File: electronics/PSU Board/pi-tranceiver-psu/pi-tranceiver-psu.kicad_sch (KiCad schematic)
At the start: 28 parts, among them IC1 LTC4368IMS-2#PBF, Q1 DMT6002LPS-13, Q2 DMT6002LPS-13

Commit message: Added 5.1V 3V supply
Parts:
- added C?: 10nF, Capacitor_SMD:C_0805_2012Metric_Pad1.18x1.45mm_HandSolder, symbol Device:C
- added C?: 220uF, CAPAE660X770N, symbol SamacSys_Parts:865080545012
- added D?: 1N5822, symbol Device:D_Schottky
- added L?: 33uH, symbol Device:L
- added R?: 3K16, Resistor_SMD:R_0805_2012Metric_Pad1.20x1.40mm_HandSolder, symbol Device:R
- added R?: 1K, Resistor_SMD:R_0805_2012Metric_Pad1.20x1.40mm_HandSolder, symbol Device:R
- added U?: LM2596S-ADJ, Package_TO_SOT_SMD:TO-263-5_TabPin3, symbol Regulator_Switching:LM2596S-ADJ
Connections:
- net GND: now also C?.2, D?.2 (A), R?.2, U?.3 (GND)
- net at C3.1, C5.1, D?.2 (A)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: now also U?.1 (VIN), U?.5 (~{ON}/OFF)
- new net: D?.1 (K), L?.2, U?.2 (OUT)
- new net: C?.1, R?.1, R?.1, U?.4 (FB)
- new net: C?.1, C?.2, L?.1, R?.2
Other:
- note added: "13.8V Output"
- note added: "5.117V @3A"
- note added: "Input"
- moved on the sheet: C1, C2, C3, C4, C5, C?, D1, D?, IC1, Q1, Q2, Q?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

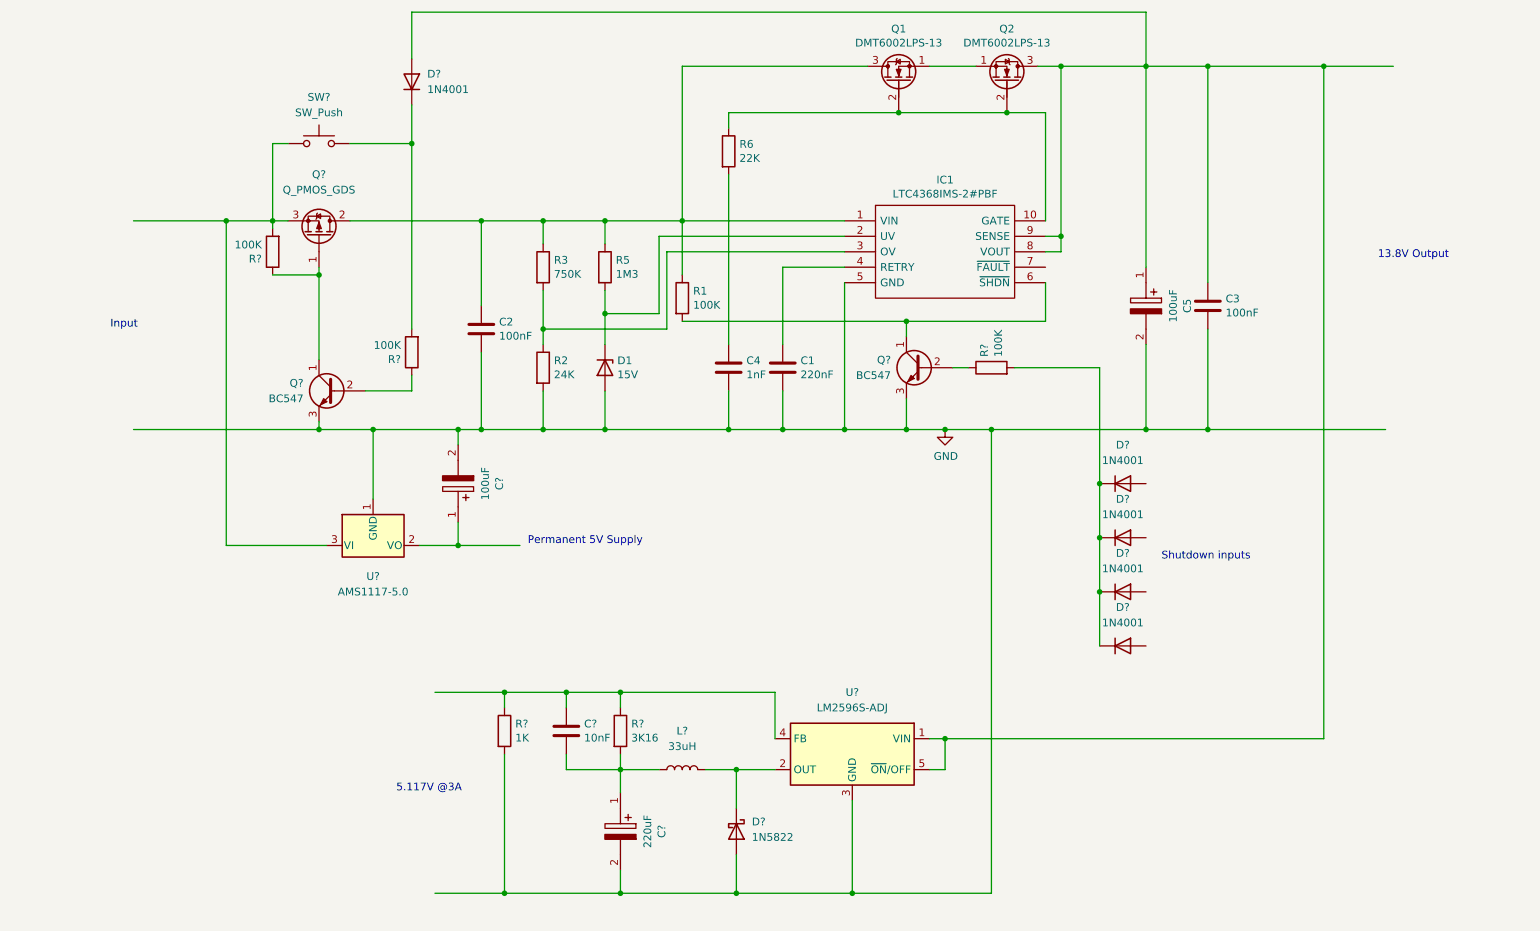
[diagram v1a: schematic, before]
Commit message: Updated shutdown circuit
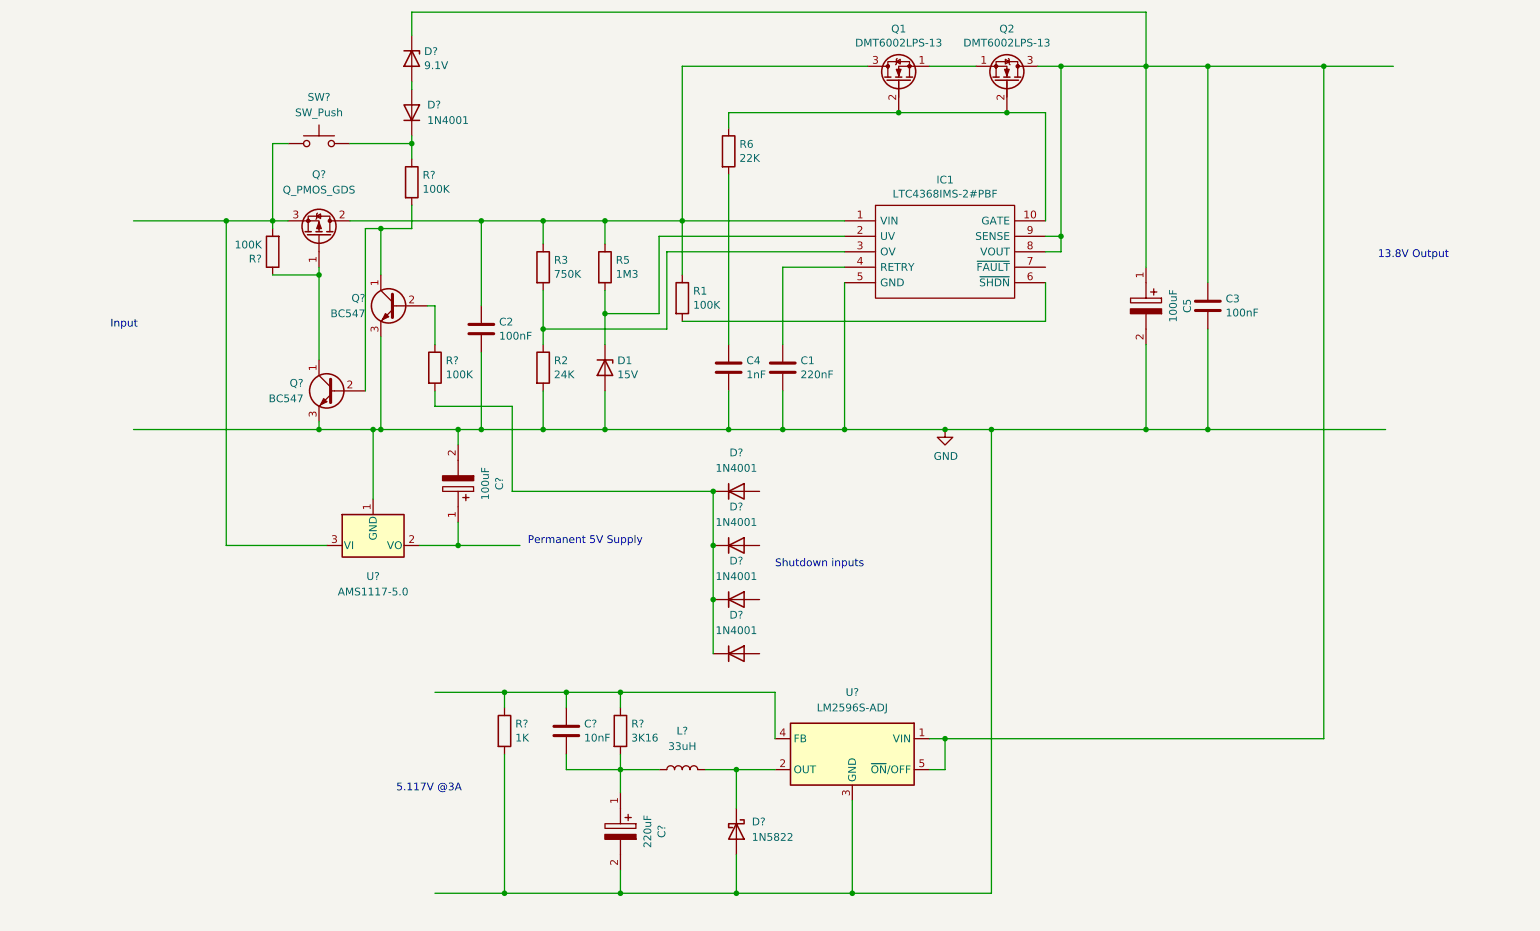
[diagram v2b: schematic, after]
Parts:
- added D?: 9.1V, Diode_SMD:D_0805_2012Metric, symbol Device:D_Zener
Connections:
- net at IC1.6 (~{SHDN}), R1.2: no longer Q?.1 (C)
- net at C3.1, C5.1, IC1.8 (VOUT)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: now also D?.1 (K); no longer D?.2 (A)
- net at R?.1: now also D?.1 (K), SW?.2; no longer Q?.2 (B)
- new net: Q?.1 (C), Q?.2 (B), R?.2
- new net: D?.2 (A), D?.2 (A)
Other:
- moved on the sheet: D?, Q?, R?

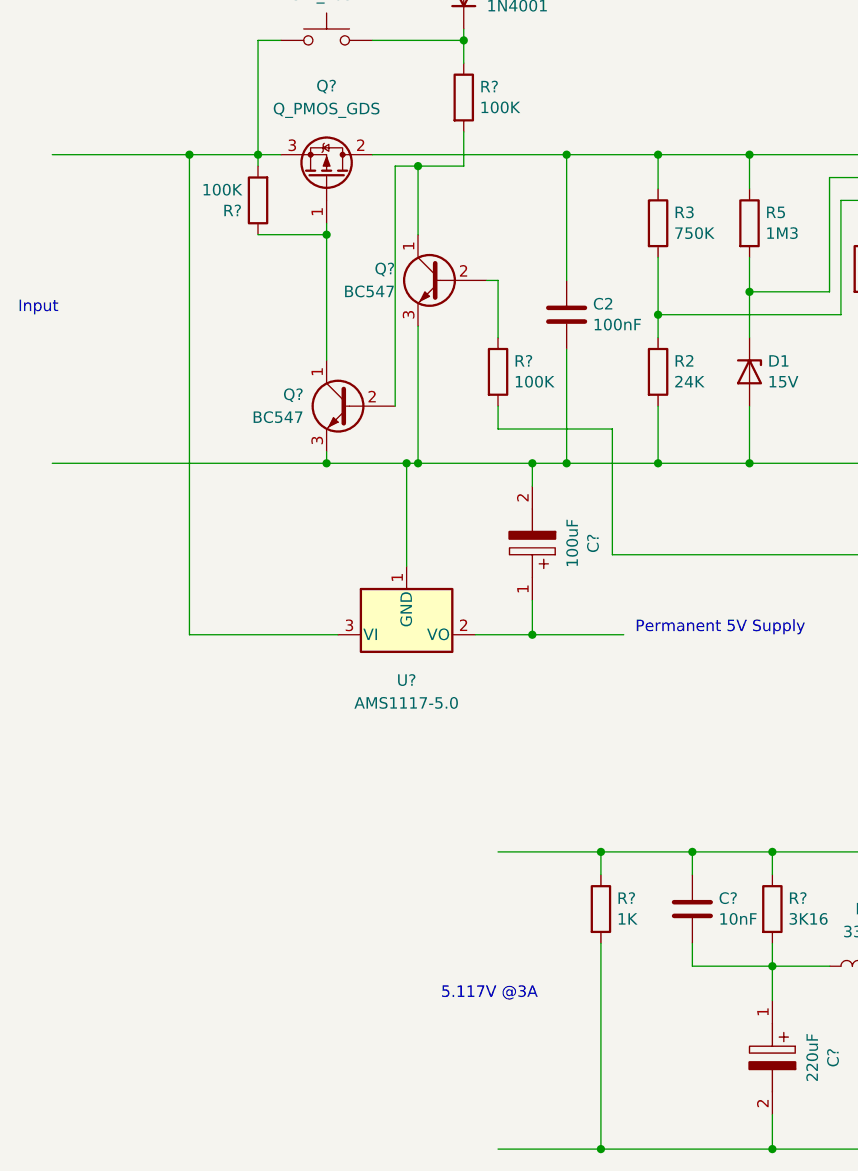
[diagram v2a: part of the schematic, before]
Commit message: Shutdown circuit update and 5v supply output fix
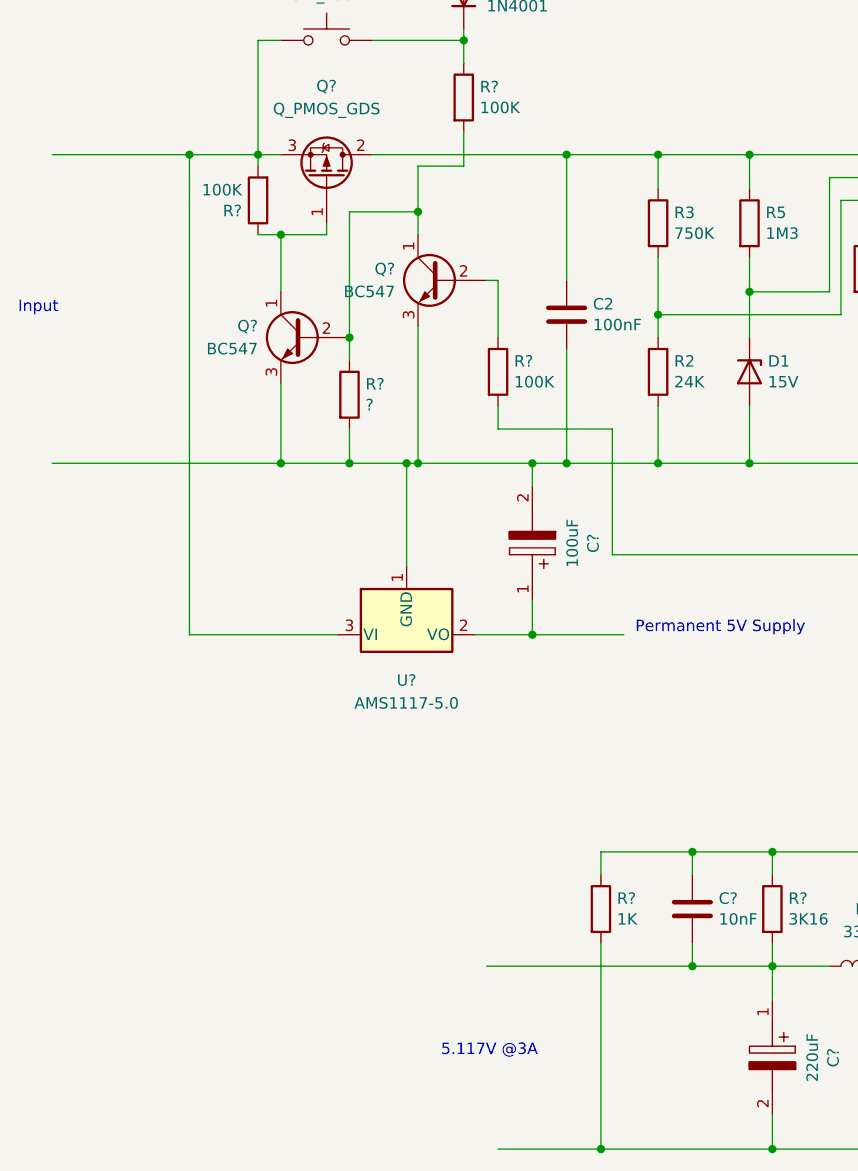
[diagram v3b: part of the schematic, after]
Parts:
- added R?: ?, Resistor_SMD:R_0805_2012Metric_Pad1.20x1.40mm_HandSolder, symbol Device:R
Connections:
- net GND: now also R?.2
- net at Q?.1 (C), Q?.2 (B), R?.2: now also R?.1
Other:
- moved on the sheet: Q?
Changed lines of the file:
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@@
   (junction (at 207.01 85.09) (diameter 0) (color 0 0 0 0)
   )
-  (junction (at 81.28 52.07) (diameter 0) (color 0 0 0 0)
-  )
-  (junction (at 71.12 85.09) (diameter 0) (color 0 0 0 0)
-  )
   (junction (at 217.17 85.09) (diameter 0) (color 0 0 0 0)
   )
@@
   (junction (at 139.7 161.29) (diameter 0) (color 0 0 0 0)
   )
+  (junction (at 73.66 85.09) (diameter 0) (color 0 0 0 0)
+  )
   (junction (at 63.5 50.8) (diameter 0) (color 0 0 0 0)
   )
@@
   (junction (at 93.98 104.14) (diameter 0) (color 0 0 0 0)
   )
+  (junction (at 111.76 140.97) (diameter 0) (color 0 0 0 0)
+  )
   (junction (at 118.11 66.04) (diameter 0) (color 0 0 0 0)
   )
@@
   (junction (at 101.6 161.29) (diameter 0) (color 0 0 0 0)
   )
-  (junction (at 71.12 59.69) (diameter 0) (color 0 0 0 0)
+  (junction (at 66.04 85.09) (diameter 0) (color 0 0 0 0)
+  )
+  (junction (at 73.66 71.12) (diameter 0) (color 0 0 0 0)
   )
   (junction (at 97.79 85.09) (diameter 0) (color 0 0 0 0)
@@
   (junction (at 173.99 85.09) (diameter 0) (color 0 0 0 0)
   )
+  (junction (at 66.04 59.69) (diameter 0) (color 0 0 0 0)
+  )
   (junction (at 157.48 85.09) (diameter 0) (color 0 0 0 0)
   )
@@
   (junction (at 93.98 85.09) (diameter 0) (color 0 0 0 0)
   )
+  (junction (at 81.28 57.15) (diameter 0) (color 0 0 0 0)
+  )
   (junction (at 120.65 161.29) (diameter 0) (color 0 0 0 0)
   )
@@
   (junction (at 184.15 33.02) (diameter 0) (color 0 0 0 0)
   )
-  (junction (at 101.6 128.27) (diameter 0) (color 0 0 0 0)
-  )
   (wire (pts (xy 146.05 135.89) (xy 146.05 128.27))
     (stroke (width 0) (type default) (color 0 0 0 0))
@@
     (stroke (width 0) (type default) (color 0 0 0 0))
   )
-  (wire (pts (xy 63.5 59.69) (xy 71.12 59.69))
+  (wire (pts (xy 63.5 59.69) (xy 66.04 59.69))
     (stroke (width 0) (type default) (color 0 0 0 0))
   )
@@
     (stroke (width 0) (type default) (color 0 0 0 0))
   )
-  (wire (pts (xy 78.74 52.07) (xy 81.28 52.07))
-    (stroke (width 0) (type default) (color 0 0 0 0))
-  )
   (wire (pts (xy 190.5 50.8) (xy 190.5 33.02))
     (stroke (width 0) (type default) (color 0 0 0 0))
@@
     (stroke (width 0) (type default) (color 0 0 0 0))
   )
-  (wire (pts (xy 71.12 59.69) (xy 71.12 73.66))
-    (stroke (width 0) (type default) (color 0 0 0 0))
-  )
-  (wire (pts (xy 71.12 85.09) (xy 80.01 85.09))
+  (wire (pts (xy 40.64 85.09) (xy 66.04 85.09))
     (stroke (width 0) (type default) (color 0 0 0 0))
   )
@@
     (stroke (width 0) (type default) (color 0 0 0 0))
   )
-  (wire (pts (xy 81.28 52.07) (xy 81.28 59.69))
+  (wire (pts (xy 81.28 52.07) (xy 81.28 57.15))
     (stroke (width 0) (type default) (color 0 0 0 0))
   )
@@
     (stroke (width 0) (type default) (color 0 0 0 0))
   )
+  (wire (pts (xy 111.76 140.97) (xy 88.9 140.97))
+    (stroke (width 0) (type default) (color 0 0 0 0))
+  )
   (wire (pts (xy 101.6 161.29) (xy 120.65 161.29))
     (stroke (width 0) (type default) (color 0 0 0 0))
@@
     (stroke (width 0) (type default) (color 0 0 0 0))
   )
+  (wire (pts (xy 73.66 85.09) (xy 80.01 85.09))
+    (stroke (width 0) (type default) (color 0 0 0 0))
+  )
   (wire (pts (xy 107.95 50.8) (xy 118.11 50.8))
     (stroke (width 0) (type default) (color 0 0 0 0))
@@
     (stroke (width 0) (type default) (color 0 0 0 0))
   )
-  (wire (pts (xy 40.64 85.09) (xy 71.12 85.09))
-    (stroke (width 0) (type default) (color 0 0 0 0))
-  )
   (wire (pts (xy 120.65 128.27) (xy 111.76 128.27))
     (stroke (width 0) (type default) (color 0 0 0 0))
@@
     (stroke (width 0) (type default) (color 0 0 0 0))
   )
+  (wire (pts (xy 81.28 57.15) (xy 81.28 59.69))
+    (stroke (width 0) (type default) (color 0 0 0 0))
+  )
   (wire (pts (xy 63.5 38.1) (xy 66.04 38.1))
     (stroke (width 0) (type default) (color 0 0 0 0))
@@
     (stroke (width 0) (type default) (color 0 0 0 0))
   )
-  (wire (pts (xy 90.17 128.27) (xy 101.6 128.27))
-    (stroke (width 0) (type default) (color 0 0 0 0))
-  )
   (wire (pts (xy 102.87 81.28) (xy 90.17 81.28))
     (stroke (width 0) (type default) (color 0 0 0 0))
@@
     (stroke (width 0) (type default) (color 0 0 0 0))
   )
+  (wire (pts (xy 66.04 76.2) (xy 66.04 85.09))
+    (stroke (width 0) (type default) (color 0 0 0 0))
+  )
   (wire (pts (xy 190.5 53.34) (xy 193.04 53.34))
     (stroke (width 0) (type default) (color 0 0 0 0))
@@
     (stroke (width 0) (type default) (color 0 0 0 0))
   )
+  (wire (pts (xy 66.04 59.69) (xy 71.12 59.69))
+    (stroke (width 0) (type default) (color 0 0 0 0))
+  )
+  (wire (pts (xy 73.66 57.15) (xy 81.28 57.15))
+    (stroke (width 0) (type default) (color 0 0 0 0))
+  )
   (wire (pts (xy 120.65 161.29) (xy 139.7 161.29))
     (stroke (width 0) (type default) (color 0 0 0 0))
@@
     (stroke (width 0) (type default) (color 0 0 0 0))
   )
-  (wire (pts (xy 71.12 83.82) (xy 71.12 85.09))
-    (stroke (width 0) (type default) (color 0 0 0 0))
-  )
   (wire (pts (xy 127 53.34) (xy 127 66.04))
     (stroke (width 0) (type default) (color 0 0 0 0))
@@
     (stroke (width 0) (type default) (color 0 0 0 0))
   )
+  (wire (pts (xy 66.04 59.69) (xy 66.04 66.04))
+    (stroke (width 0) (type default) (color 0 0 0 0))
+  )
+  (wire (pts (xy 66.04 85.09) (xy 73.66 85.09))
+    (stroke (width 0) (type default) (color 0 0 0 0))
+  )
   (wire (pts (xy 157.48 53.34) (xy 127 53.34))
     (stroke (width 0) (type default) (color 0 0 0 0))
@@
     (stroke (width 0) (type default) (color 0 0 0 0))
   )
+  (wire (pts (xy 73.66 71.12) (xy 73.66 57.15))
+    (stroke (width 0) (type default) (color 0 0 0 0))
+  )
   (wire (pts (xy 86.36 38.1) (xy 86.36 40.64))
     (stroke (width 0) (type default) (color 0 0 0 0))
@@
     (stroke (width 0) (type default) (color 0 0 0 0))
   )
-  (wire (pts (xy 78.74 78.74) (xy 78.74 52.07))
-    (stroke (width 0) (type default) (color 0 0 0 0))
-  )
   (wire (pts (xy 130.81 50.8) (xy 157.48 50.8))
     (stroke (width 0) (type default) (color 0 0 0 0))
@@
     (stroke (width 0) (type default) (color 0 0 0 0))
   )
+  (wire (pts (xy 73.66 81.28) (xy 73.66 85.09))
+    (stroke (width 0) (type default) (color 0 0 0 0))
+  )
   (wire (pts (xy 101.6 128.27) (xy 101.6 130.81))
     (stroke (width 0) (type default) (color 0 0 0 0))
@@
   )
   (wire (pts (xy 236.22 25.4) (xy 236.22 135.89))
+    (stroke (width 0) (type default) (color 0 0 0 0))
+  )
+  (wire (pts (xy 73.66 71.12) (xy 73.66 73.66))
     (stroke (width 0) (type default) (color 0 0 0 0))
   )
@@
     (effects (font (size 1.27 1.27)) (justify left bottom))
   )
-  (text "5.117V @3A" (at 83.82 144.78 0)
+  (text "5.117V @3A" (at 83.82 151.13 0)
     (effects (font (size 1.27 1.27)) (justify left bottom))
   )
@@
     (pin "2")
   )
+  (symbol (lib_id "Device:R") (at 73.66 77.47 0) (unit 1)
+    (in_bom yes) (on_board yes)
+    (property "Reference" "R?" (id 0) (at 75.438 76.3016 0)
+      (effects (font (size 1.27 1.27)) (justify left))
+    )
+    (property "Value" "?" (id 1) (at 75.438 78.613 0)
+      (effects (font (size 1.27 1.27)) (justify left))
+    )
+    (property "Footprint" "Resistor_SMD:R_0805_2012Metric_Pad1.20x1.40mm_HandSolder" (id 2) (at 71.882 77.47 90)
+      (effects (font (size 1.27 1.27)) hide)
+    )
+    (property "Datasheet" "~" (id 3) (at 73.66 77.47 0)
+      (effects (font (size 1.27 1.27)) hide)
+    )
+    (pin "1")
+    (pin "2")
+  )
   (symbol (lib_id "SamacSys_Parts:865080545012") (at 120.65 144.78 270) (unit 1)
     (in_bom yes) (on_board yes)
@@
     (pin "2")
   )
-  (symbol (lib_id "Transistor_BJT:BC547") (at 73.66 78.74 0) (mirror y) (unit 1)
+  (symbol (lib_id "Transistor_BJT:BC547") (at 68.58 71.12 0) (mirror y) (unit 1)
     (in_bom yes) (on_board yes) (fields_autoplaced)
-    (property "Reference" "Q?" (id 0) (at 68.58 77.4699 0)
-      (effects (font (size 1.27 1.27)) (justify left))
-    )
-    (property "Value" "BC547" (id 1) (at 68.58 80.0099 0)
-      (effects (font (size 1.27 1.27)) (justify left))
-    )
-    (property "Footprint" "Package_TO_SOT_THT:TO-92_Inline" (id 2) (at 68.58 80.645 0)
+    (property "Reference" "Q?" (id 0) (at 63.5 69.8499 0)
+      (effects (font (size 1.27 1.27)) (justify left))
+    )
+    (property "Value" "BC547" (id 1) (at 63.5 72.3899 0)
+      (effects (font (size 1.27 1.27)) (justify left))
+    )
+    (property "Footprint" "Package_TO_SOT_THT:TO-92_Inline" (id 2) (at 63.5 73.025 0)
       (effects (font (size 1.27 1.27) italic) (justify left) hide)
     )
-    (property "Datasheet" "https://www.onsemi.com/pub/Collateral/BC550-D.pdf" (id 3) (at 73.66 78.74 0)
+    (property "Datasheet" "https://www.onsemi.com/pub/Collateral/BC550-D.pdf" (id 3) (at 68.58 71.12 0)
       (effects (font (size 1.27 1.27)) (justify left) hide)
     )
@@
       (reference "R?") (unit 1) (value "1K") (footprint "Resistor_SMD:R_0805_2012Metric_Pad1.20x1.40mm_HandSolder")
     )
+    (path "/8f84e6d3-48fe-4eae-96c7-940f1c338ac4"
+      (reference "R?") (unit 1) (value "?") (footprint "Resistor_SMD:R_0805_2012Metric_Pad1.20x1.40mm_HandSolder")
+    )
     (path "/d5e38fca-598b-4d8a-98c9-6da71b070d70"
